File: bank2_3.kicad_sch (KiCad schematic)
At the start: 9 parts, among them U1 ECP5-BGA256

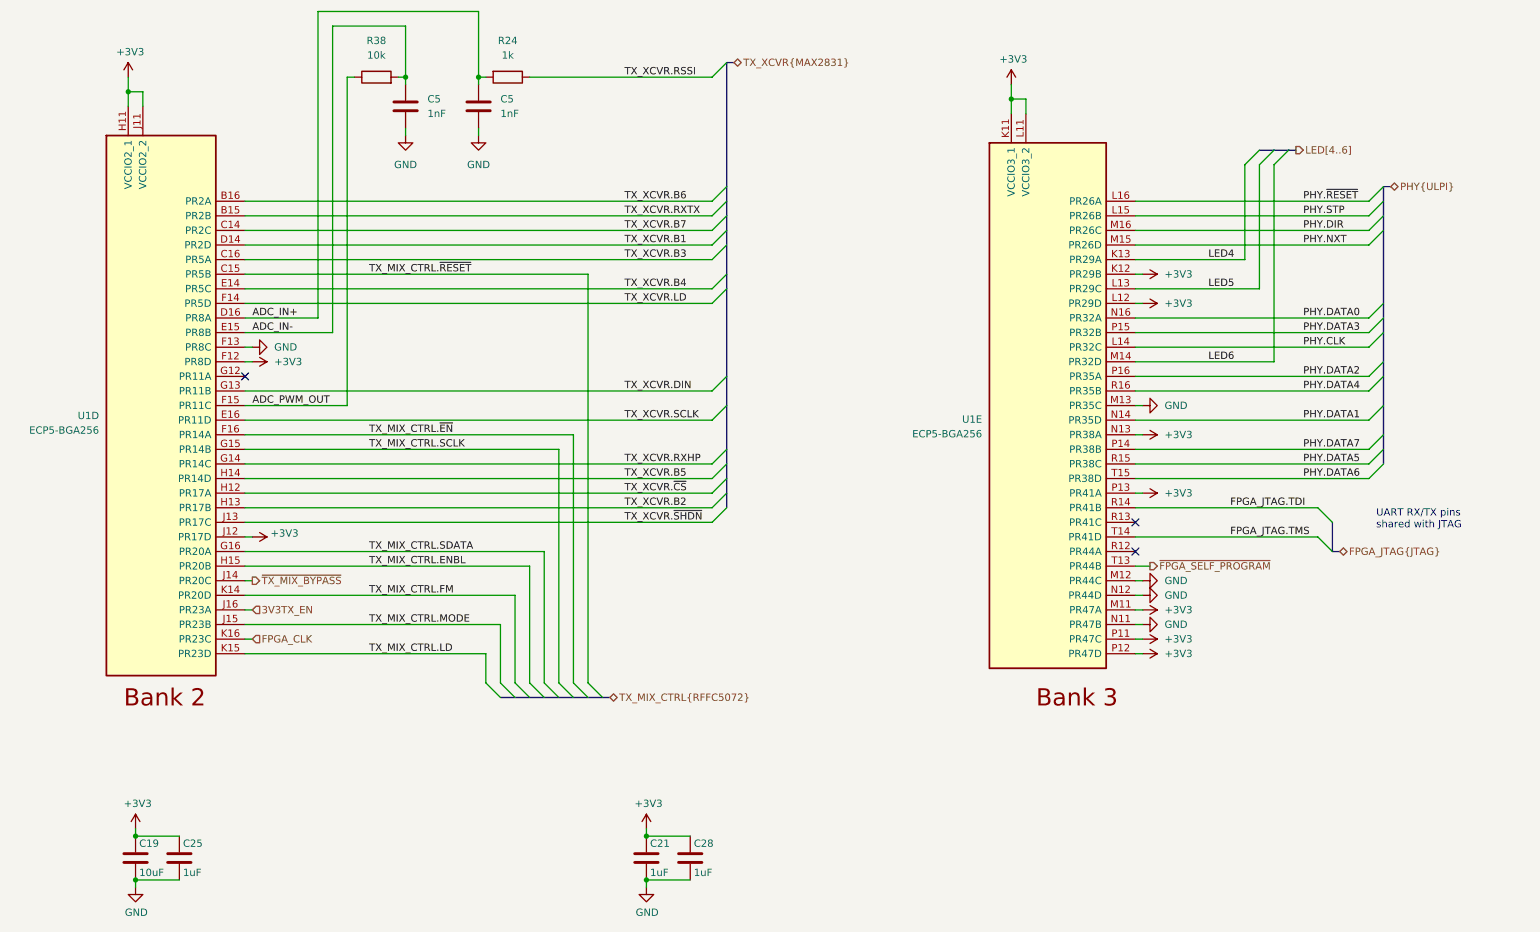
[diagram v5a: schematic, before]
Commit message: complete initial layout
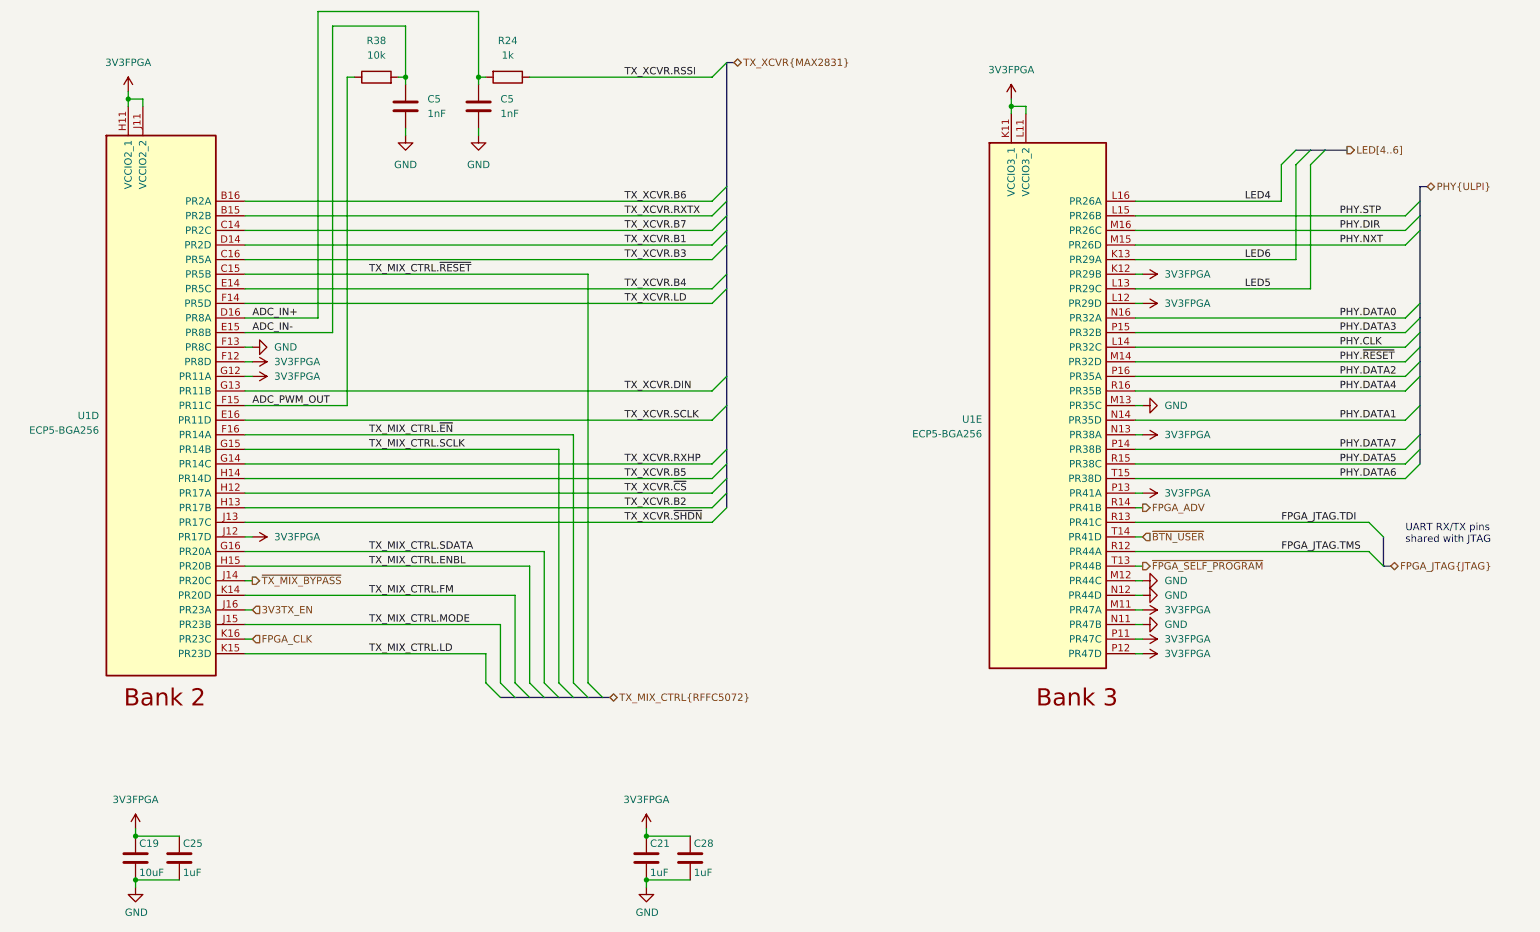
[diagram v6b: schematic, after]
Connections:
- net +3V3 is gone; now on net 3V3FPGA: C19.1, C21.1, C25.1, C28.1, U1.F12 (PR8D), U1.H11 (VCCIO2_1), U1.J11 (VCCIO2_2), U1.J12 (PR17D), U1.K11 (VCCIO3_1), U1.K12 (PR29B), U1.L11 (VCCIO3_2), U1.L12 (PR29D), U1.M11 (PR47A), U1.N13 (PR38A), U1.P11 (PR47C), U1.P12 (PR47D), U1.P13 (PR41A)
- net FPGA_JTAG.TDI: now also U1.R13 (PR41C); no longer U1.R14 (PR41B)
- net FPGA_JTAG.TMS: now also U1.R12 (PR44A); no longer U1.T14 (PR41D)
- net LED4: now also U1.L16 (PR26A); no longer U1.K13 (PR29A)
- net LED6: now also U1.K13 (PR29A); no longer U1.M14 (PR32D)
- net PHY.~{RESET}: now also U1.M14 (PR32D); no longer U1.L16 (PR26A)
- net 3V3FPGA: now reaches U1.G12 (PR11A)
- new net FPGA_ADV: U1.R14 (PR41B)
- new net ~{BTN_USER}: U1.T14 (PR41D)
- no-connect marks 3 -> 0
